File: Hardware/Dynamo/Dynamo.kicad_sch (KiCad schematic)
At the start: 46 parts, among them U1 AP63205WU, U10 ESP32-S3-WROOM-1, U11 NCP1117-3.3_SOT223, U13 TXS0102DCT, U14 TXS0102DCT, U2 TLP2770, U3 TLP2770, U4 74LVC1G86, U5 74LVC1G86, U6 74LVC1G86, U7 74LVC1G86, U8 74LVC1G86, U9 74LVC1G86

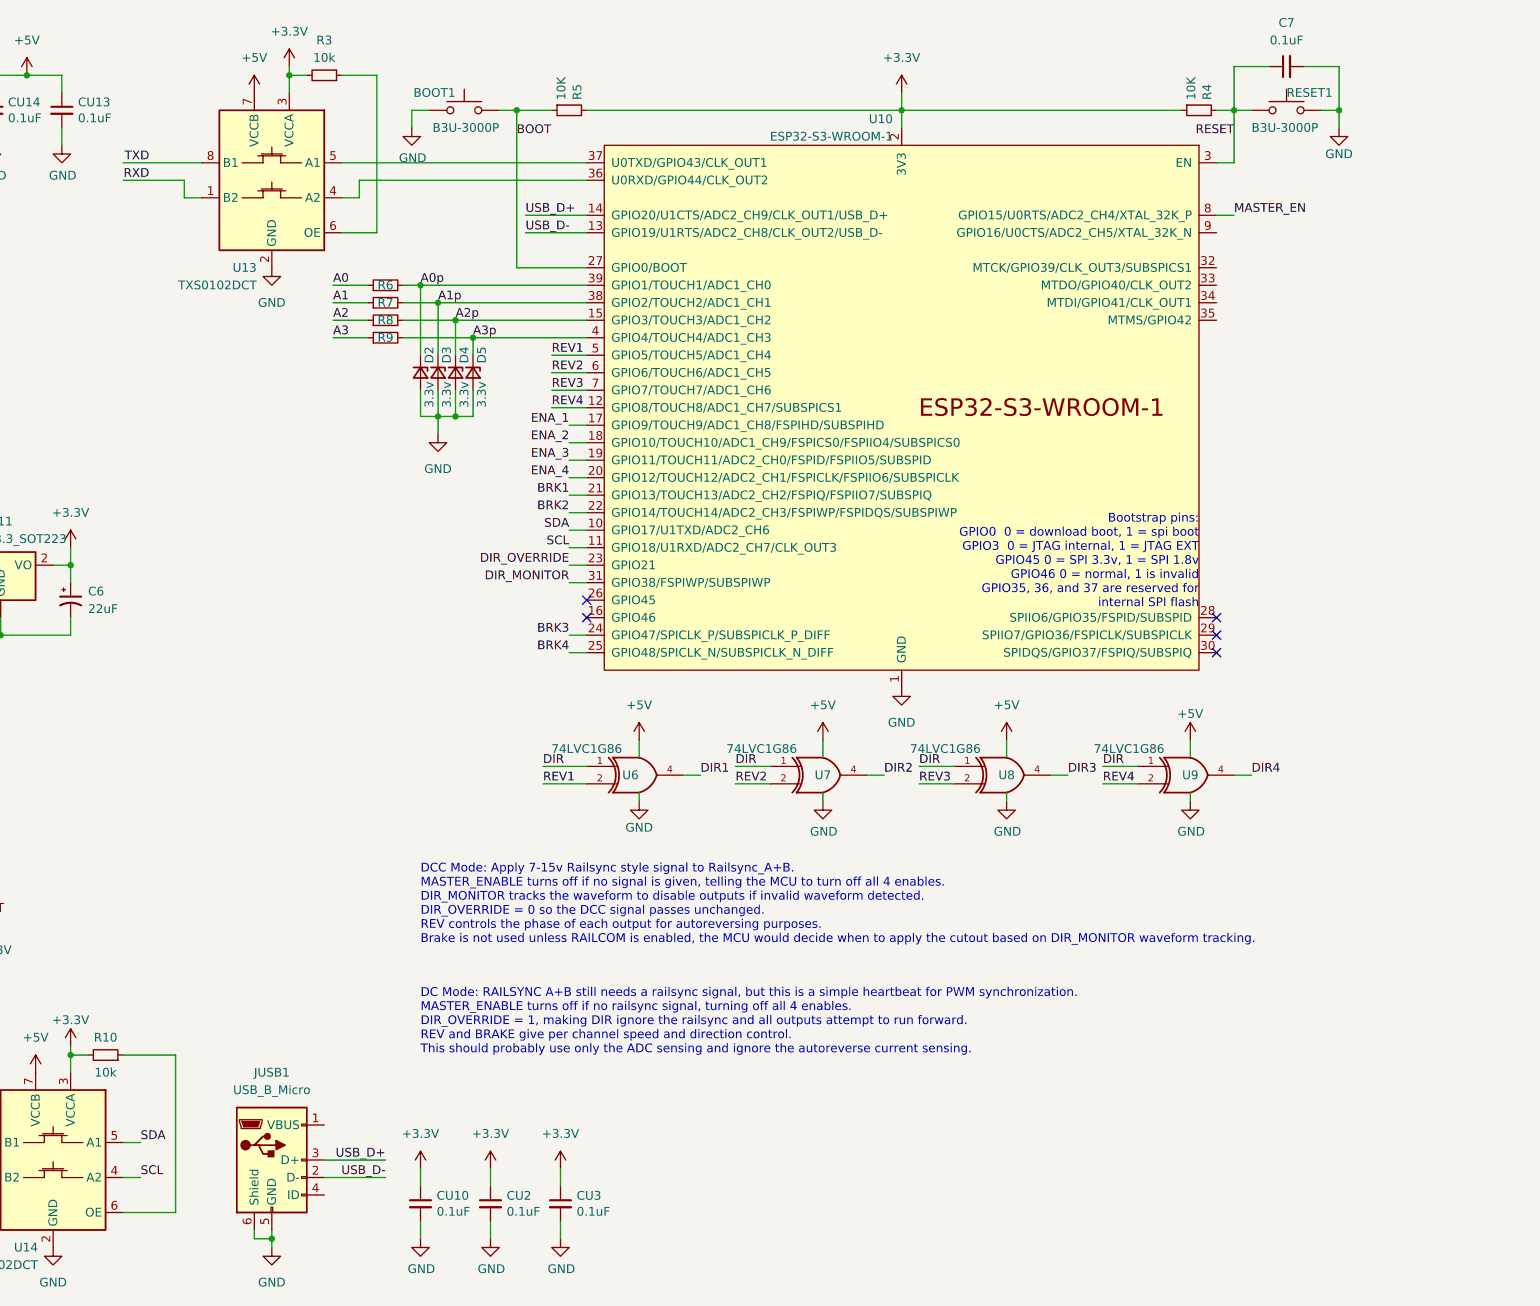
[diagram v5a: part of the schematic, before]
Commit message: Schematic features changed: Added USB power for programming, per-track DC mode gating. New PCB layout improving on previous builds.
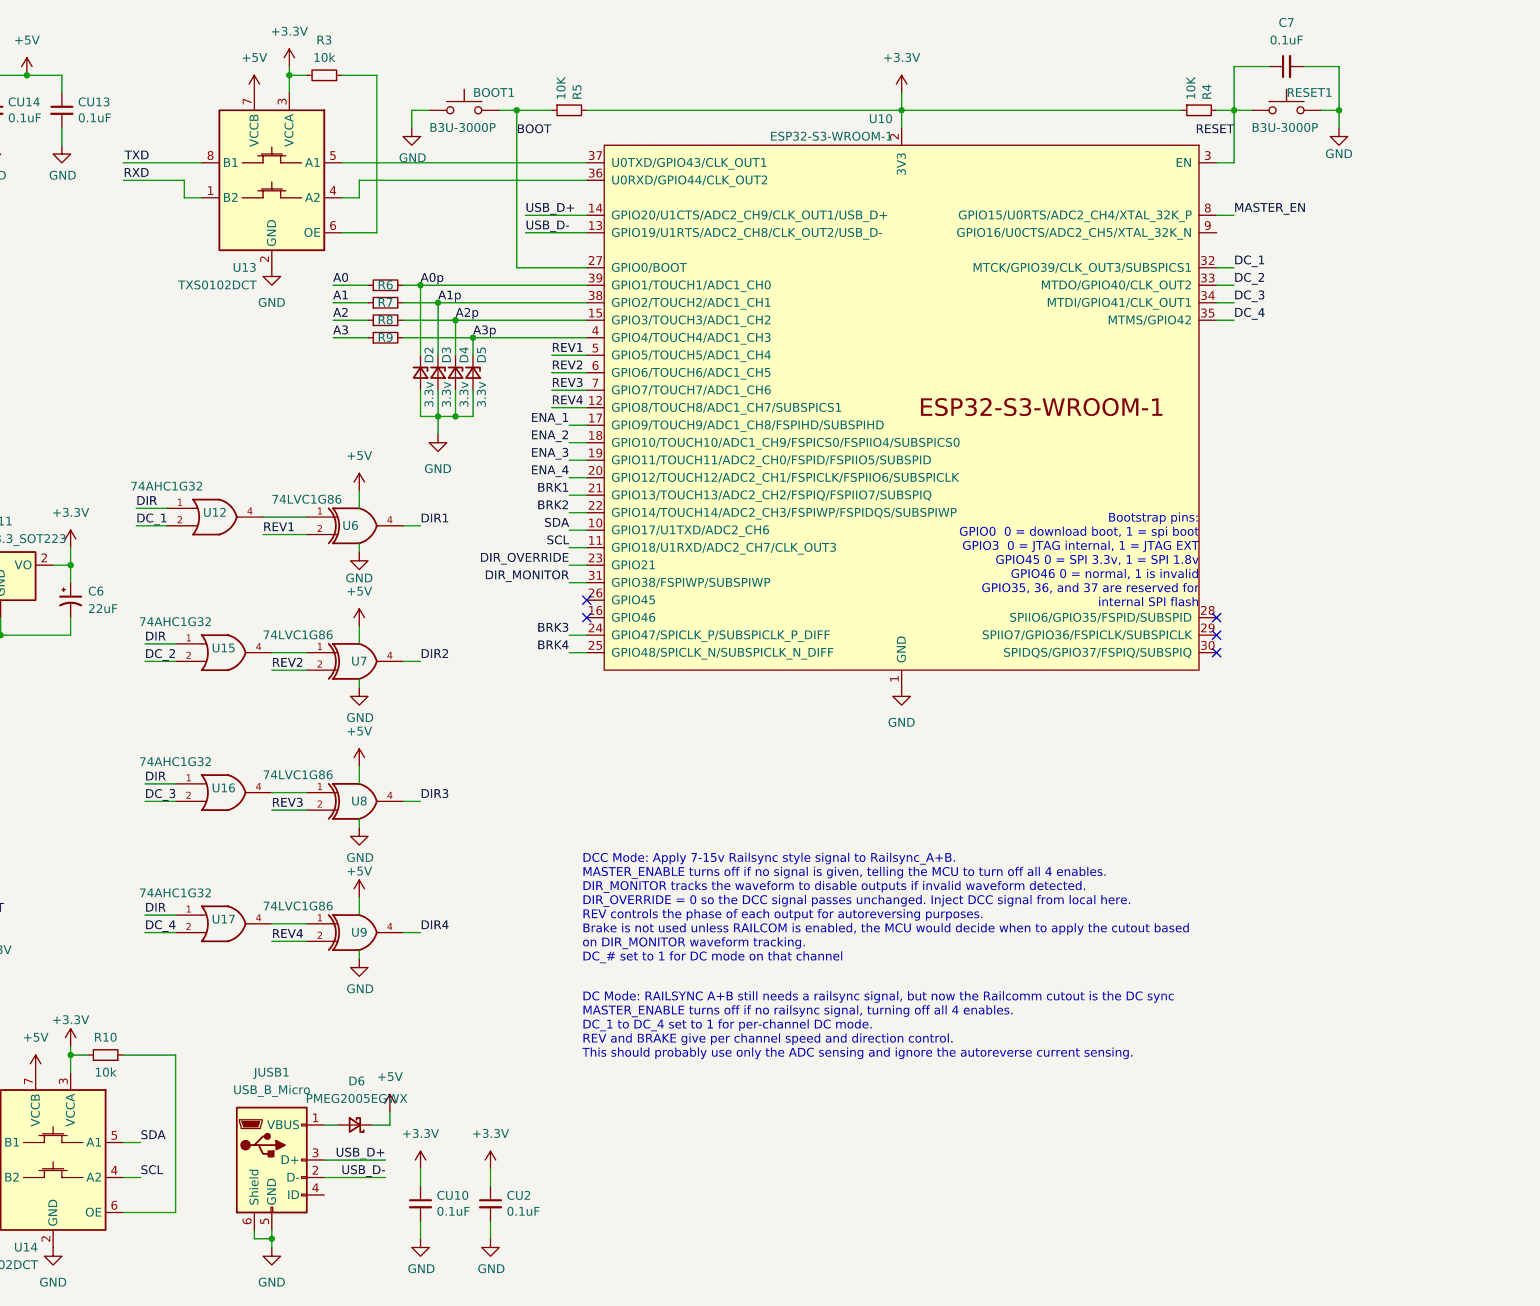
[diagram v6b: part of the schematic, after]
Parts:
- removed CU3: 0.1uF, Capacitor_SMD:C_1206_3216Metric, symbol Device:C_Small
- added D6: PMEG2005EGWX, Diode_SMD:D_SOD-123, symbol Device:D_Schottky_Small
- added U12, U15, U16, U17: 74AHC1G32, Package_TO_SOT_SMD:SOT-23-5_HandSoldering, symbol Loconet DCC Interface-rescue:74AHC1G32-74xGxx
- BOOT1, RESET1: footprint Button_Switch_SMD:SW_SPST_B3U-3000P -> Button_Switch_SMD:SW_SPST_B3U-3000P-B
- U10: footprint Espressif:ESP32-S3-WROOM-1U -> Espressif:ESP32-S3-WROOM-1
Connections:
- net +5V: now also D6.1 (K), U12.5 (VCC), U15.5 (VCC), U16.5 (VCC), U17.5 (VCC)
- net BOOT: now also BOOT1.1; no longer BOOT1.2
- net DIR: now also U12.1, U15.1, U16.1, U17.1; no longer U6.1, U7.1, U8.1, U9.1
- net GND: now also BOOT1.2, U12.3 (GND), U15.3 (GND), U16.3 (GND), U17.3 (GND); no longer BOOT1.1
- net at JUSB1.1 (VBUS): now also D6.2 (A)
- net DC_1: now reaches U10.32 (MTCK/GPIO39/CLK_OUT3/SUBSPICS1)
- net DC_1: now also U12.2
- net DC_2: now reaches U10.33 (MTDO/GPIO40/CLK_OUT2)
- net DC_2: now also U15.2
- net DC_3: now reaches U10.34 (MTDI/GPIO41/CLK_OUT1)
- net DC_3: now also U16.2
- net DC_4: now reaches U10.35 (MTMS/GPIO42)
- net DC_4: now also U17.2
- new net: U12.4, U6.1
- new net: U15.4, U7.1
- new net: U16.4, U8.1
- new net: U17.4, U9.1
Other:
- note added: "DC Mode: RAILSYNC A+B still needs a railsync signal, but now the Railcomm cutout is the DC sync MASTER_ENABLE turns off if no railsync signal, turning off all 4 enables. DC_1 to DC_4 set to 1 for per-channel DC mode. REV and BRAKE give per channel speed and direction control. This should probably use only the ADC sensing and ignore the autoreverse current sensing."
- note added: "DCC Mode: Apply 7-15v Railsync style signal to Railsync_A+B. MASTER_ENABLE turns off if no signal is given, telling the MCU to turn off all 4 enables. DIR_MONITOR tracks the waveform to disable outputs if invalid waveform detected. DIR_OVERRIDE = 0 so the DCC signal passes unchanged. Inject DCC signal from local here. REV controls the phase of each output for autoreversing purposes. Brake is not 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"
- note removed: "DC Mode: RAILSYNC A+B still needs a railsync signal, but this is a simple heartbeat for PWM synchronization. MASTER_ENABLE turns off if no railsync signal, turning off all 4 enables. DIR_OVERRIDE = 1, making DIR ignore the railsync and all outputs attempt to run forward. REV and BRAKE give per channel speed and direction control. This should probably use only the ADC sensing and ignore the autore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"
- note removed: "DCC Mode: Apply 7-15v Railsync style signal to Railsync_A+B. MASTER_ENABLE turns off if no signal is given, telling the MCU to turn off all 4 enables. DIR_MONITOR tracks the waveform to disable outputs if invalid waveform detected. DIR_OVERRIDE = 0 so the DCC signal passes unchanged. REV controls the phase of each output for autoreversing purposes. Brake is not used unless RAILCOM is enabled, the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"
- moved on the sheet: U6, U7, U8, U9

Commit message: Recheck Schematic/PCB for inconsistencies
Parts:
- BOOT1, RESET1: JLCPCB Part # (none) -> C963349
- C1: JLCPCB Part # (none) -> C2223641
- C2, C4, C5, C6: JLCPCB Part # (none) -> C2164091
- C3, C7, CU10, CU13, CU14, CU2: JLCPCB Part # (none) -> C600013
- D1: JLCPCB Part # (none) -> C7164018
- D2, D3, D4, D5: JLCPCB Part # (none) -> C151564
- D6: JLCPCB Part # (none) -> C552812
- JUSB1: JLCPCB Part # (none) -> C136000
- R1: JLCPCB Part # (none) -> C132648
- R10, R3, R4, R5: JLCPCB Part # (none) -> C4303232
- R2, R6, R7, R8, R9: JLCPCB Part # (none) -> C131398
- Railsync1: JLCPCB Part # (none) -> C5140626
- U1: JLCPCB Part # (none) -> C2071056
- U10: JLCPCB Part # (none) -> C2980298
- U11: JLCPCB Part # (none) -> C91728
- U12, U15, U16, U17: JLCPCB Part # (none) -> C10096
- U13, U14: JLCPCB Part # (none) -> C2677354
- U2, U3: JLCPCB Part # (none) -> C150160
- U4, U5, U6, U7, U8, U9: JLCPCB Part # (none) -> C402161

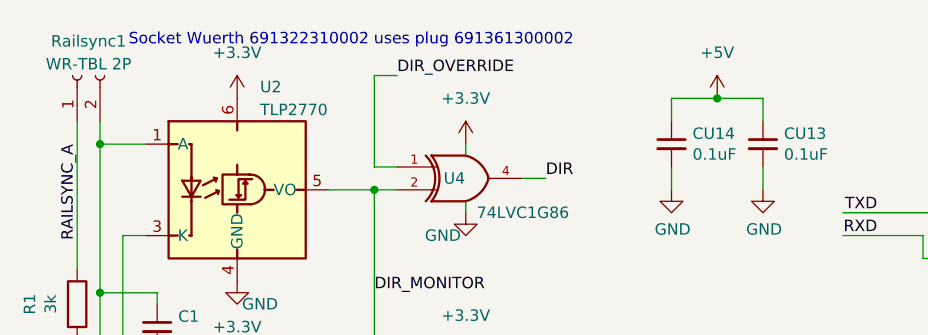
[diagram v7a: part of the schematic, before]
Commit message: Change Railsync input to use same 3.5mm connector as EX8874 outputs
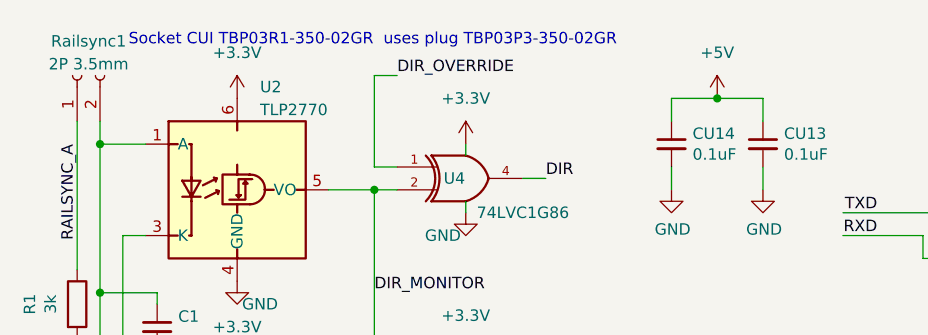
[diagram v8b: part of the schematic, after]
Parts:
- Railsync1: value WR-TBL 2P -> 2P 3.5mm; footprint Terminal_Wuerth_new:WR-TBL 2P -> Connector_Phoenix_MC:PhoenixContact_MC_1,5_2-G-3.5_1x02_P3.50mm_Horizontal; JLCPCB Part # C5140626 -> C880572; MFG Wuerth -> CUI Inc; PN 691322310002 -> TBP03R1-350-02GR
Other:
- note added: "Socket CUI TBP03R1-350-02GR uses plug TBP03P3-350-02GR"
- note removed: "Socket Wuerth 691322310002 uses plug 691361300002"
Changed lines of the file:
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@@
     (effects (font (size 1.27 1.27)) (justify left bottom))
   )
-  (text "Socket Wuerth 691322310002 uses plug 691361300002" (at 26.035 14.605 0)
+  (text "Socket CUI TBP03R1-350-02GR  uses plug TBP03P3-350-02GR\n"
+    (at 26.035 14.605 0)
     (effects (font (size 1.27 1.27)) (justify left bottom))
   )
@@
       (effects (font (size 1.27 1.27)))
     )
-    (property "Value" "WR-TBL 2P" (at 21.59 16.51 90)
-      (effects (font (size 1.27 1.27)))
-    )
-    (property "Footprint" "Terminal_Wuerth_new:WR-TBL 2P" (at 20.32 17.78 0)
+    (property "Value" "2P 3.5mm" (at 21.59 16.51 90)
+      (effects (font (size 1.27 1.27)))
+    )
+    (property "Footprint" "Connector_Phoenix_MC:PhoenixContact_MC_1,5_2-G-3.5_1x02_P3.50mm_Horizontal" (at 20.32 17.78 0)
       (effects (font (size 1.27 1.27)) hide)
     )
@@
       (effects (font (size 1.27 1.27)) hide)
     )
-    (property "MFG" "Wuerth" (at 20.32 17.78 0)
-      (effects (font (size 1.27 1.27)) hide)
-    )
-    (property "PN" "691322310002 " (at 20.32 17.78 0)
-      (effects (font (size 1.27 1.27)) hide)
-    )
-    (property "JLCPCB Part #" "C5140626" (at 20.32 17.78 0)
-      (effects (font (size 1.27 1.27)) hide)
-    )
+    (property "MFG" "CUI Inc" (at 20.32 17.78 0)
+      (effects (font (size 1.27 1.27)) hide)
+    )
+    (property "PN" "TBP03R1-350-02GR " (at 20.32 17.78 0)
+      (effects (font (size 1.27 1.27)) hide)
+    )
+    (property "JLCPCB Part #" "C880572" (at 20.32 17.78 0)
+      (effects (font (size 1.27 1.27)) hide)
+    )
